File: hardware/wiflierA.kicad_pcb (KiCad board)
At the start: 2 copper layers, 37.8 x 21.5 mm, 61 parts, among them CN1 10p, J1 AVRISP6, P1 WS2812, P10 SCL, P11 3V, P12 GND, P13 LED, P14 LED, P15 LED, P16 BAT, P17 TOUT, P18 AVRA0, P2 M0, P21 B+, P24 B-, P3 M1, P32 ESP_UART, P4 M2, P5 M3, P6 ANT, P9 SDA, Q1 7A_20V, Q2 7A_20V, Q3 7A_20V, Q4 7A_20V, U1 MCP1824/3.3, U2 MCP1824/3.3, U3 MPL3115A2, U4 LSM9DS1, U5 ESP8266EX, U6 W25Q80DV, U7 ATTINY441-QFN, X1 26MHz

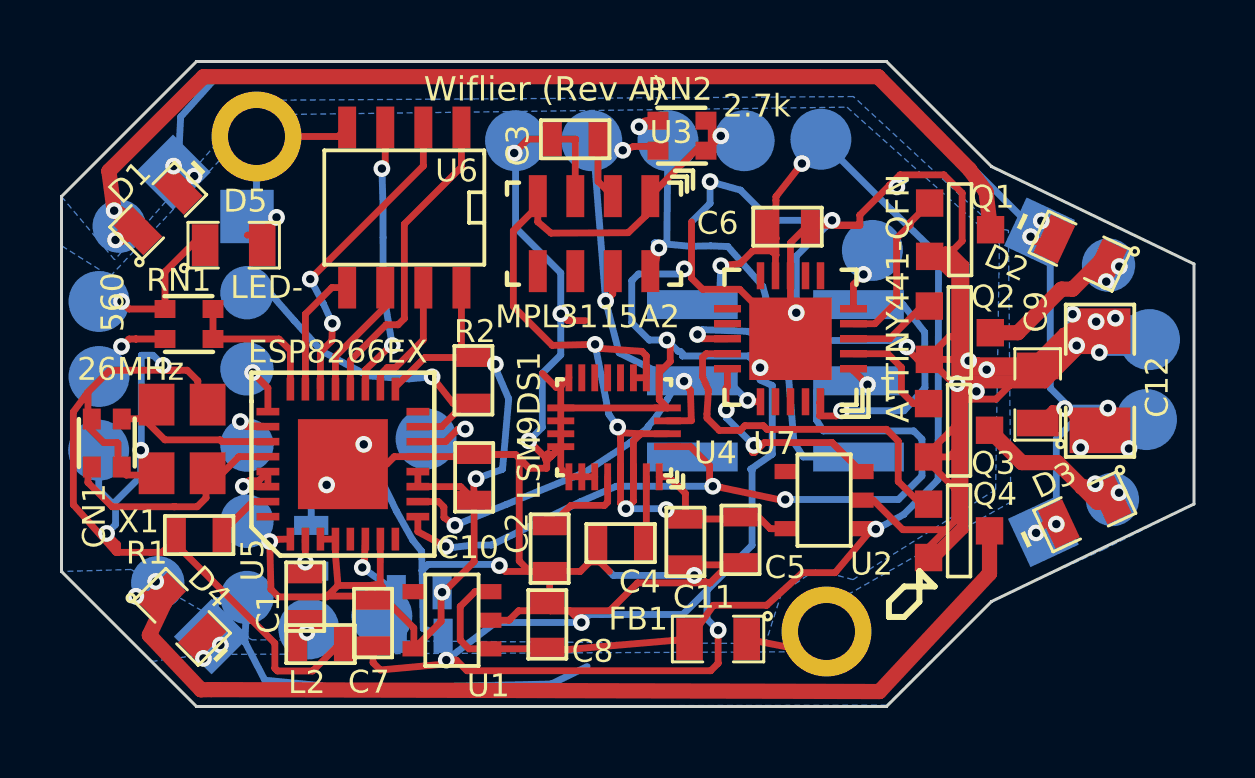
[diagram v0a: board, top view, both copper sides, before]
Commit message: Update with driver for hand-held controllers
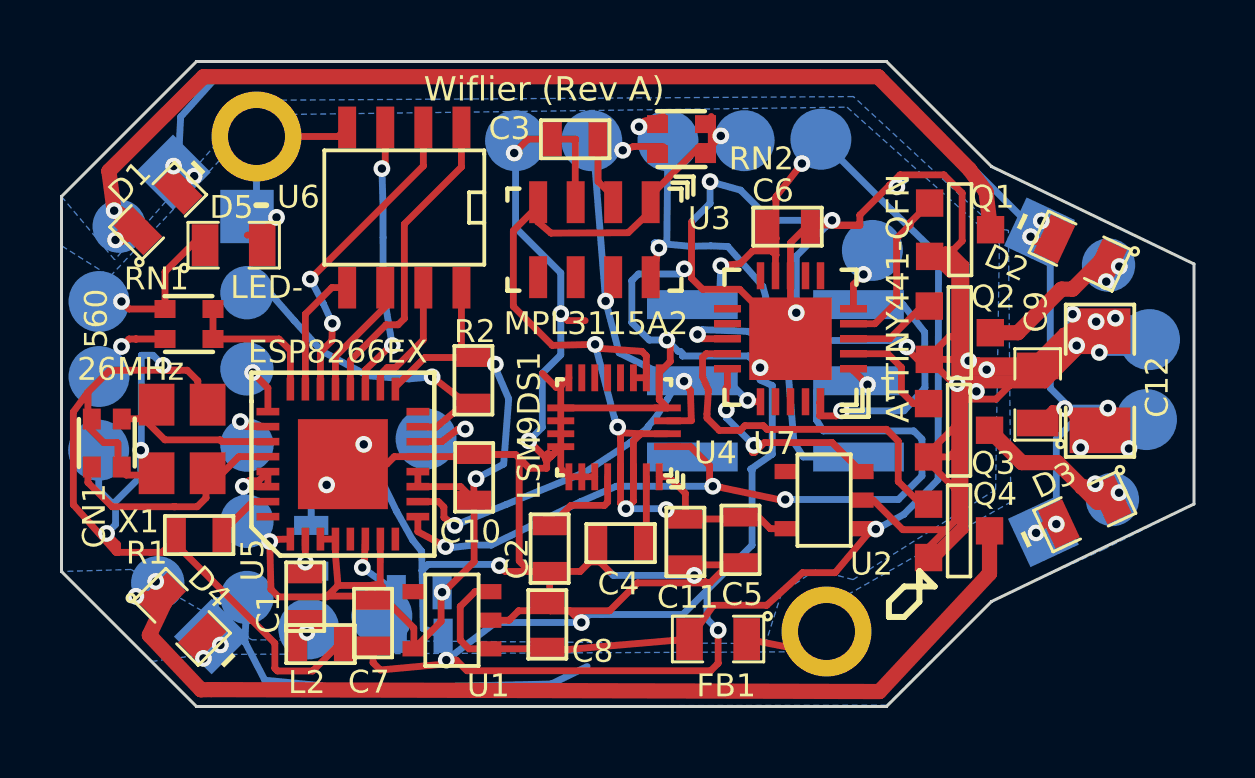
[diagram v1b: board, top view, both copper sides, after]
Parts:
- P15: value LED -> GND
- P16: value BAT -> FLTBAT
- R4: value 12k -> NP
- moved U3 0.20 mm to (63.2, 55.1)
- moved RN2 0.12 mm to (66.1, 51.8)
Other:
- board text added: "AVRMISO"
- board text added: "AVR_RST"
- board text added: "FLT_BAT"
- board text added: "SCL"
- board text added: "SDA"
